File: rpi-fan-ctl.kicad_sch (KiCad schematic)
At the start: 21 parts, among them J2 Conn_01x05, Q1 NPN, Q2 NPN, Q3 NPN, Q4 NPN

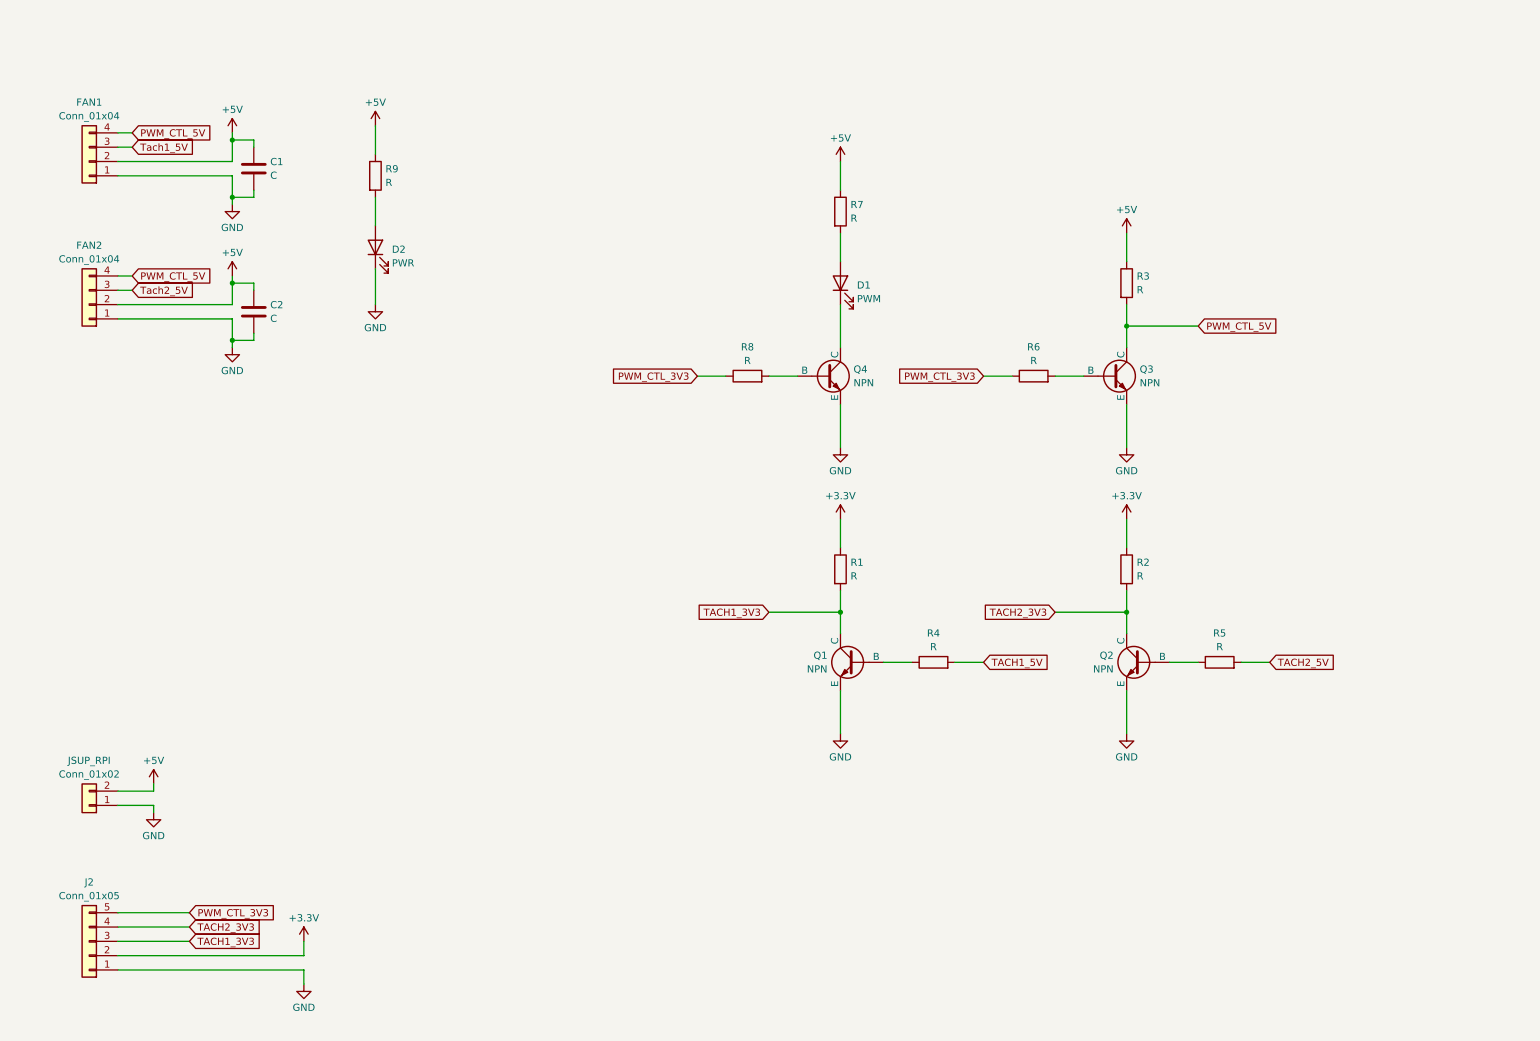
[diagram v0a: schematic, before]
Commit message: added footprints
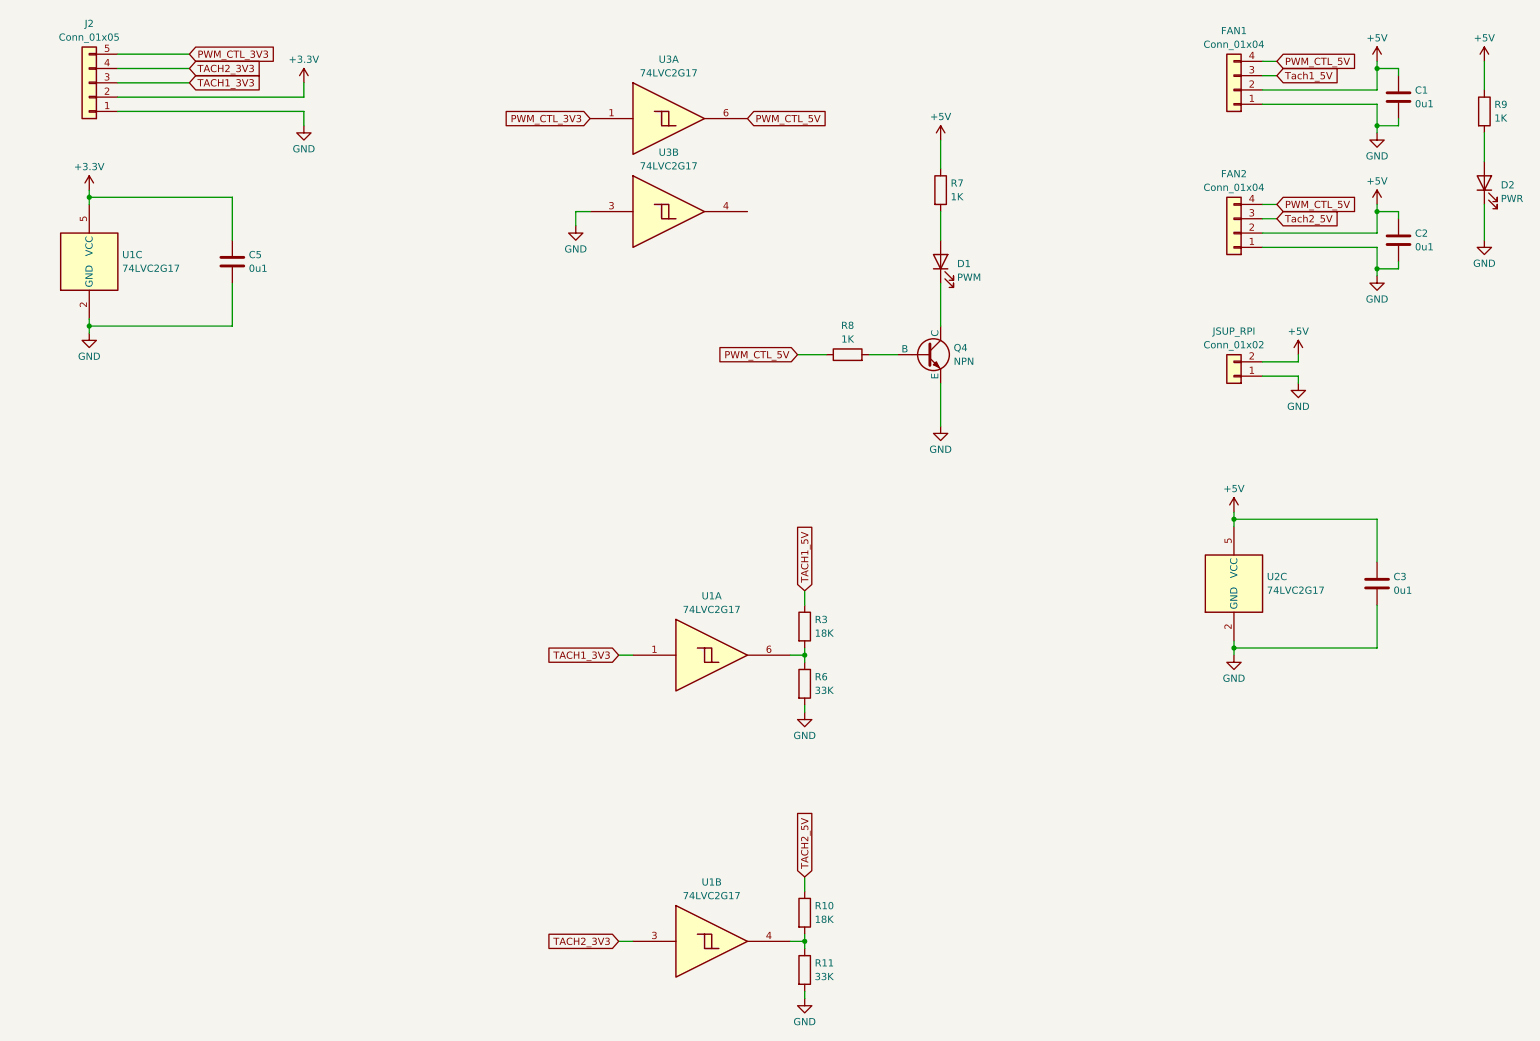
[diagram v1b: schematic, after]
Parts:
- removed Q1, Q2, Q3: NPN, symbol Simulation_SPICE:NPN
- removed R1, R2, R4, R5: R, symbol Device:R
- added C3, C5: 0u1, Capacitor_SMD:C_0603_1608Metric_Pad1.08x0.95mm_HandSolder, symbol Device:C
- added R10: 18K, Resistor_SMD:R_0603_1608Metric_Pad0.98x0.95mm_HandSolder, symbol Device:R
- added R11: 33K, Resistor_SMD:R_0603_1608Metric_Pad0.98x0.95mm_HandSolder, symbol Device:R
- added U1, U3: 74LVC2G17, Package_TO_SOT_SMD:SOT-363_SC-70-6_Handsoldering, symbol 74xGxx:74LVC2G17
- added U2: 74LVC2G17, symbol 74xGxx:74LVC2G17
- C1, C2: value C -> 0u1; footprint (none) -> Capacitor_SMD:C_0603_1608Metric_Pad1.08x0.95mm_HandSolder
- R3: value R -> 18K; footprint (none) -> Resistor_SMD:R_0603_1608Metric_Pad0.98x0.95mm_HandSolder
- R6: value R -> 33K; footprint (none) -> Resistor_SMD:R_0603_1608Metric_Pad0.98x0.95mm_HandSolder
- R7, R8, R9: value R -> 1K; footprint (none) -> Resistor_SMD:R_0603_1608Metric_Pad0.98x0.95mm_HandSolder
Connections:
- net +3.3V: now also C5.1, U1.5 (VCC)
- net +5V: now also C3.1, U2.5 (VCC); no longer R3.1
- net GND: now also R6.2, C3.2, C5.2, R11.2, U1.2 (GND), U2.2 (GND), U3.3
- net PWM_CTL_3V3: now also U3.1; no longer R6.1, R8.1
- net PWM_CTL_5V: now also R8.1, U3.6; no longer R3.2
- net TACH1_3V3: now also U1.1
- net TACH1_5V: now also R3.1
- net TACH2_3V3: now also U1.3
- net TACH2_5V: now also R10.1
- new net: R3.2, R6.1, U1.6
- new net: R10.2, R11.1, U1.4
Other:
- moved on the sheet: C1, C2, D1, D2, FAN1, FAN2, J2, JSUP_RPI, Q4, R7, R8, R9

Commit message: some routing progress
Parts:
- removed D1: PWM, symbol Device:LED
- removed D2: PWR, symbol Device:LED
- removed Q4: NPN, symbol Simulation_SPICE:NPN
- removed R8: 1K, Resistor_SMD:R_0603_1608Metric_Pad0.98x0.95mm_HandSolder, symbol Device:R
- added D1: D, Diode_SMD:D_SOD-123F, symbol Device:D
- added D2, D3, D5, D6: LTST-C191TBKT, Diode_SMD:D_0402_1005Metric_Pad0.77x0.64mm_HandSolder, symbol J-Link-SWD-rescue:LTST-C191TBKT-dk_LED-Indication-Discrete
- added D4: D, Diode_SMD:D_SOD-123, symbol Device:D
- added R1, R2, R3: 0R, Resistor_SMD:R_0603_1608Metric_Pad0.98x0.95mm_HandSolder, symbol Device:R
- added R6, R9: 1K, Resistor_SMD:R_0603_1608Metric_Pad0.98x0.95mm_HandSolder, symbol Device:R
- FAN1, FAN2: footprint (none) -> Connector_PinHeader_2.54mm:PinHeader_1x04_P2.54mm_Horizontal
- RPI1: renamed from J2; footprint (none) -> Connector_PinHeader_2.54mm:PinHeader_1x05_P2.54mm_Vertical
- SUP1: renamed from JSUP_RPI; footprint (none) -> Connector_PinHeader_2.54mm:PinHeader_1x02_P2.54mm_Horizontal
- U1: renamed from U3; footprint Package_TO_SOT_SMD:SOT-363_SC-70-6_Handsoldering -> Package_TO_SOT_SMD:SOT-23-6_Handsoldering; DigiKey https://www.digikey.de/en/products/detail/texas-instruments/SN74LVC2G17DCKR/479737 -> https://www.digikey.de/en/products/detail/texas-instruments/SN74LVC2G17DBVR/479735
- U1: renamed from U2; footprint (none) -> Package_TO_SOT_SMD:SOT-23-6_Handsoldering; DigiKey (none) -> https://www.digikey.de/en/products/detail/texas-instruments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
- U2: renamed from U1; footprint Package_TO_SOT_SMD:SOT-363_SC-70-6_Handsoldering -> Package_TO_SOT_SMD:SOT-23-6_Handsoldering; DigiKey https://www.digikey.de/en/products/detail/texas-instruments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 -> (none)
- U2: renamed from U1; footprint (none) -> Package_TO_SOT_SMD:SOT-23-6_Handsoldering
- renumbered C5 to C3, C3 to C4, R7 to R4, R9 to R5, R3 to R7, R6 to R8
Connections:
- net Tach1_5V is gone; now on net TACH1_5V: FAN1.3 (Pin_3)
- net Tach2_5V is gone; now on net TACH2_5V: FAN2.3 (Pin_3)
- net +5V: now also D1.1 (K), D4.1 (K); no longer R4.1
- net GND: now also D1.2 (A), D2.2, D3.2, D4.2 (A), D5.2, D6.2
- net PWM_CTL_3V3: now also R1.2; no longer RPI1.5 (Pin_5)
- net PWM_CTL_5V: now also R4.1
- net TACH1_3V3: now also U2.4, R3.2, R6.1; no longer RPI1.3 (Pin_3), U2.1
- net TACH2_3V3: now also U2.6, R2.2, R9.1; no longer RPI1.4 (Pin_4), U2.3
- net at R7.2, R8.1: now also U2.3; no longer U2.6
- net at R5.2: now also D3.1
- net at R10.2, R11.1: now also U2.1; no longer U2.4
- net at R4.2: now also D2.1
- new net: D5.1, R6.2
- new net: R1.1, RPI1.5 (Pin_5)
- new net: R3.1, RPI1.3 (Pin_3)
- new net: R2.1, RPI1.4 (Pin_4)
- new net: D6.1, R9.2
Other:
- moved on the sheet: C1, C2, FAN1, FAN2, R4, R5, U2A, U2B

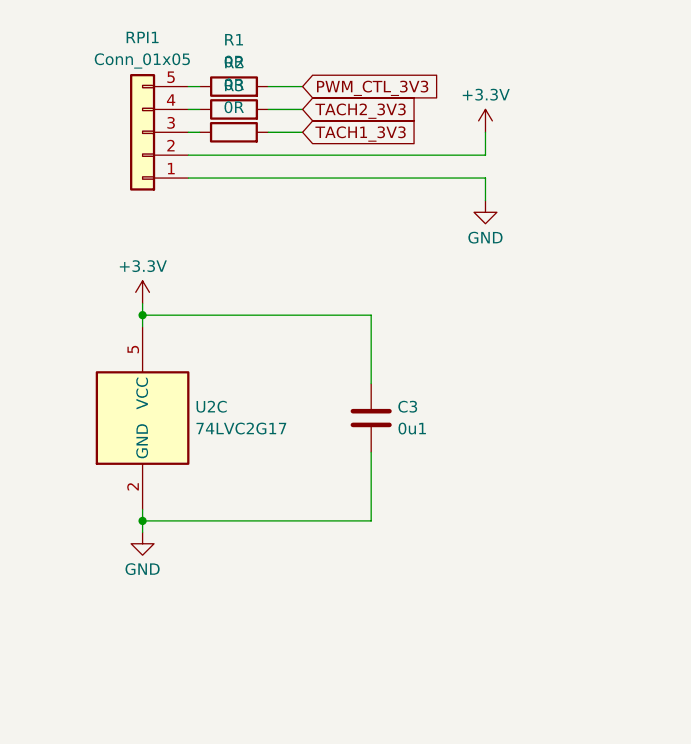
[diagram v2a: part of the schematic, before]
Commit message: made all preview connectors angled
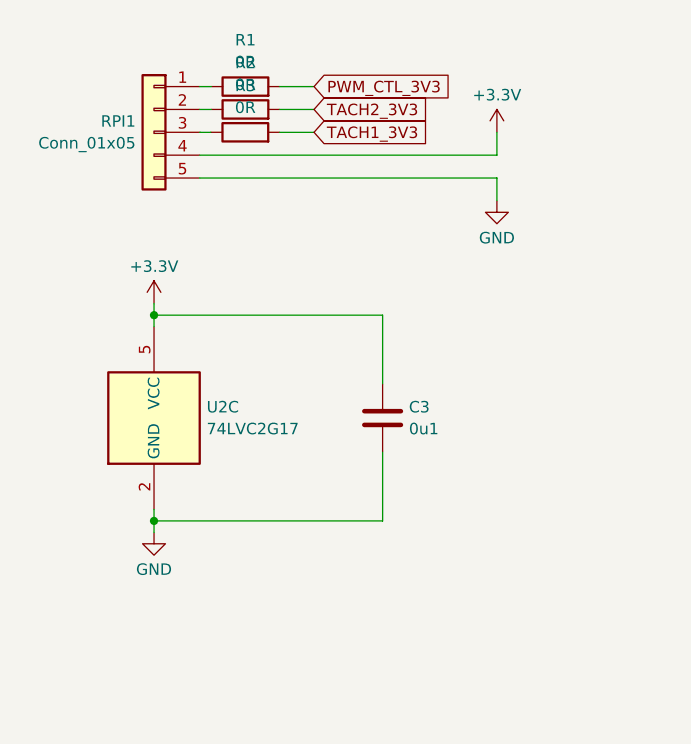
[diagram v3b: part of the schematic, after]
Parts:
- RPI1: footprint Connector_PinHeader_2.54mm:PinHeader_1x05_P2.54mm_Vertical -> Connector_PinHeader_2.54mm:PinHeader_1x05_P2.54mm_Horizontal
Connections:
- net +3.3V: now also RPI1.4 (Pin_4); no longer RPI1.2 (Pin_2)
- net GND: now also RPI1.5 (Pin_5); no longer RPI1.1 (Pin_1)
- net at R1.1: now also RPI1.1 (Pin_1); no longer RPI1.5 (Pin_5)
- net at R2.1: now also RPI1.2 (Pin_2); no longer RPI1.4 (Pin_4)
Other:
- moved on the sheet: C3, R1, R2, R3, RPI1, U2C

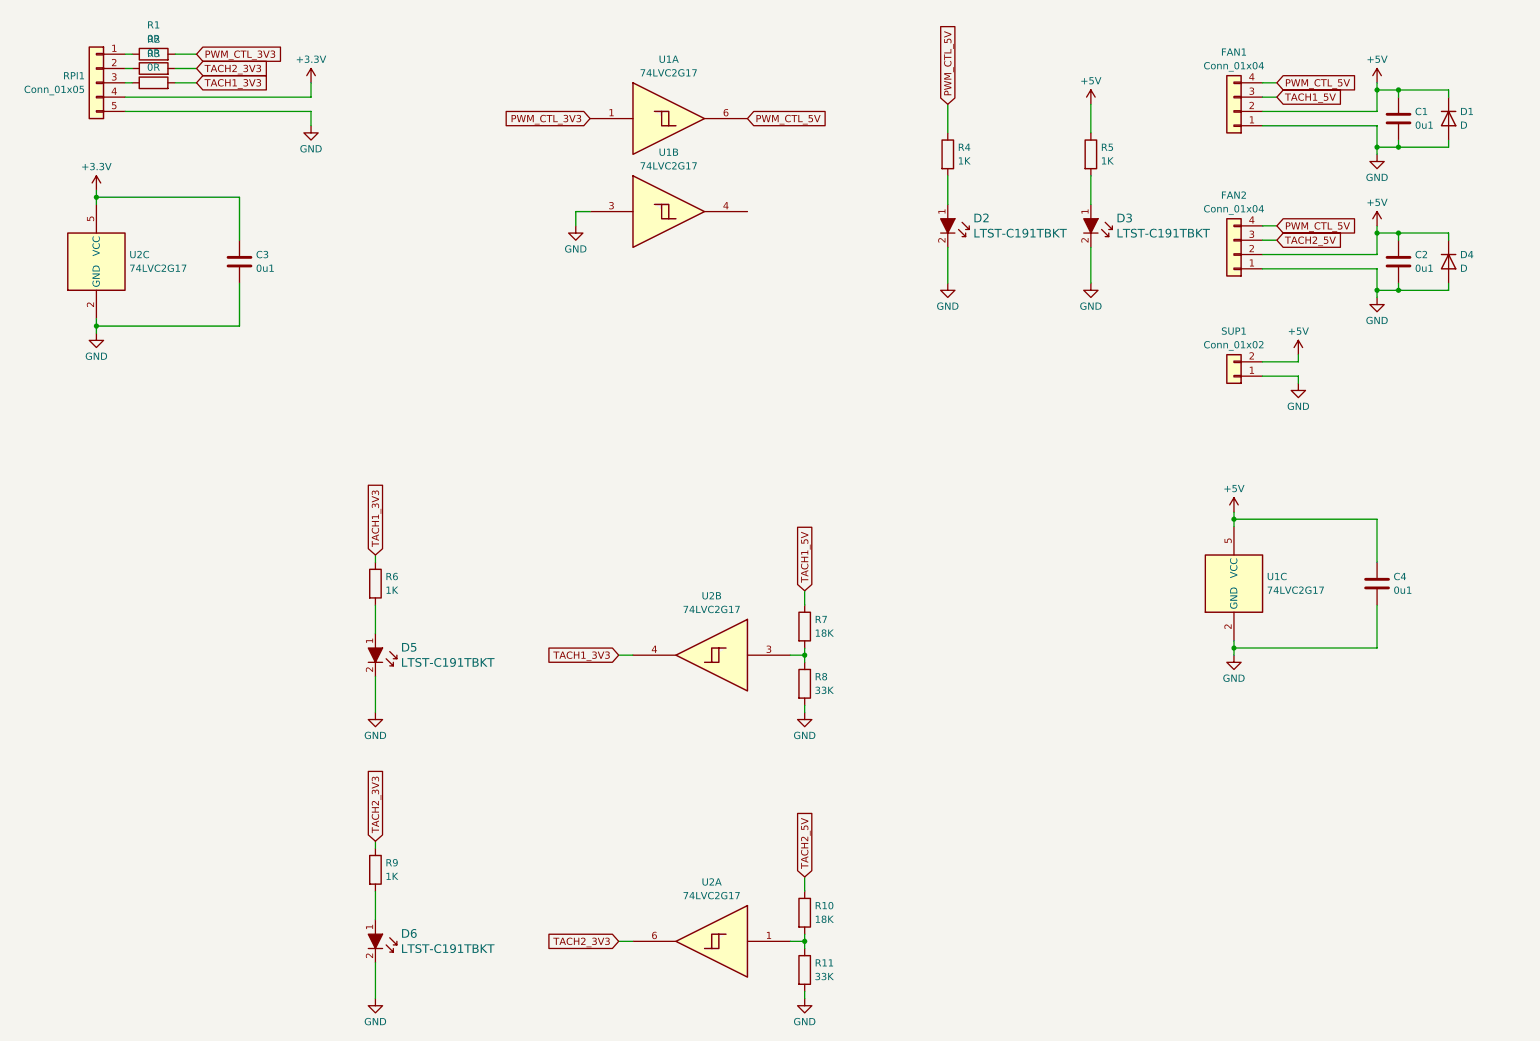
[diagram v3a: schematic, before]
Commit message: updated voltage level converter
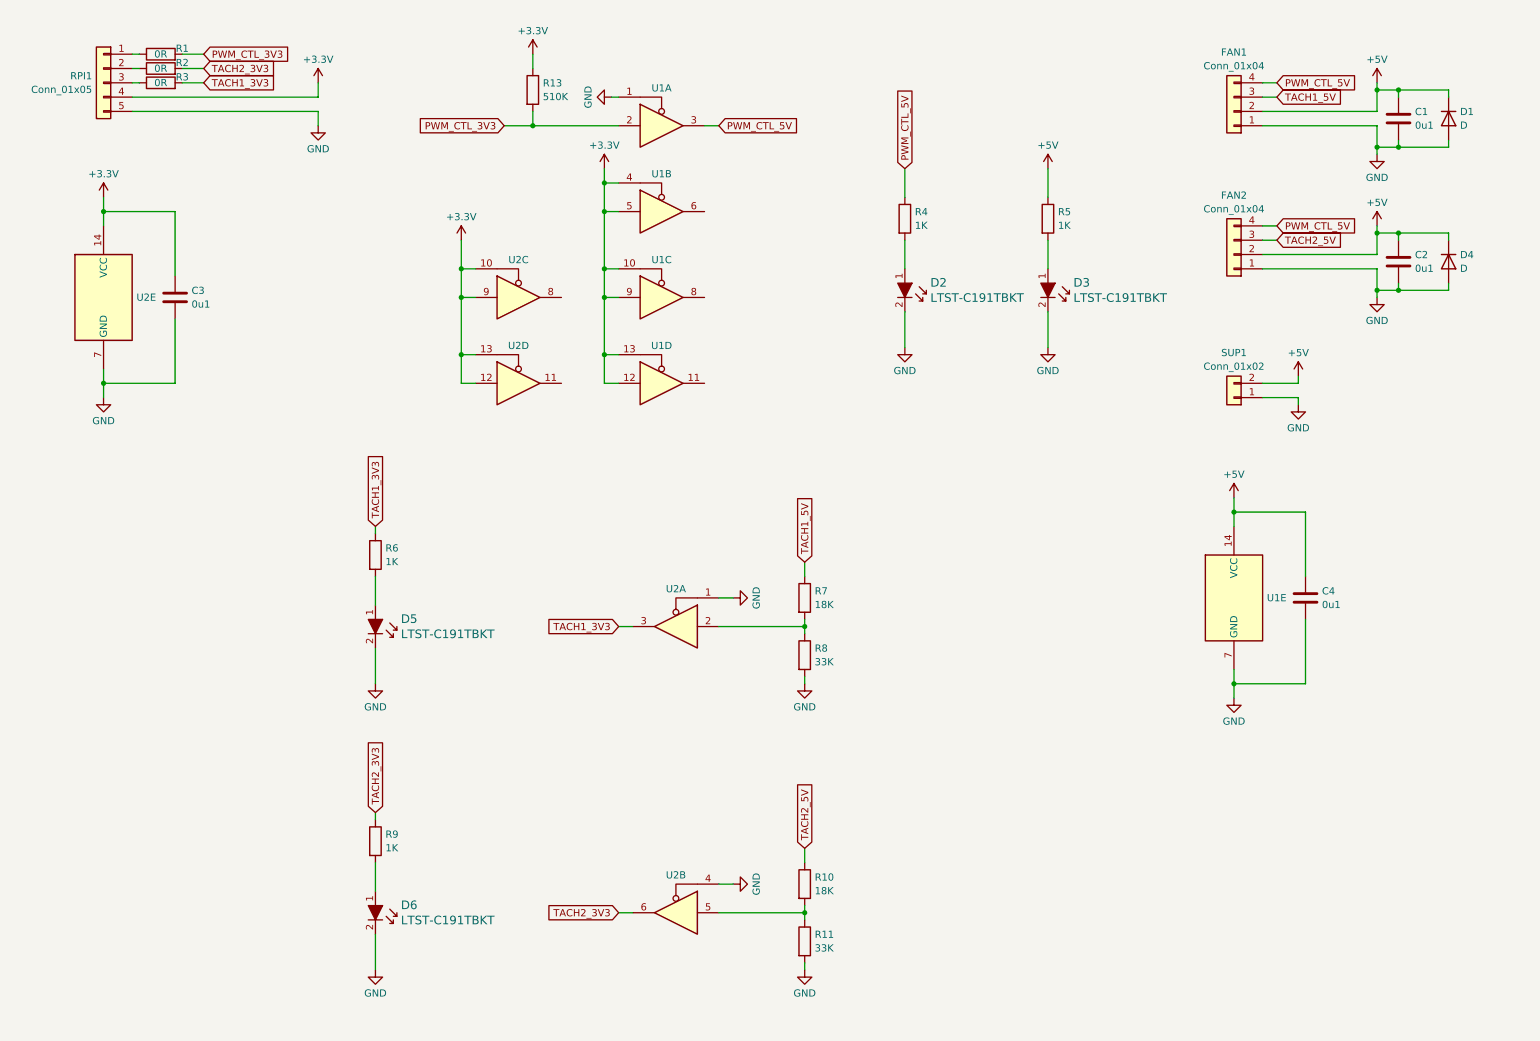
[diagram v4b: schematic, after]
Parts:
- removed U1, U2: 74LVC2G17, Package_TO_SOT_SMD:SOT-23-6_Handsoldering, symbol 74xGxx:74LVC2G17
- added R13: 510K, Resistor_SMD:R_0603_1608Metric_Pad0.98x0.95mm_HandSolder, symbol Device:R
- added U1, U2: SN74HCT125DR, Package_SO:SOIC-14_3.9x8.7mm_P1.27mm, symbol fanctl:SN74HCT125DR
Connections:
- net +3.3V: now also R13.1, U1.10, U1.12, U1.13, U1.4, U1.5, U1.9, U2.10, U2.12, U2.13, U2.14 (VCC), U2.9
- net +5V: now also U1.14 (VCC)
- net GND: now also U1.1, U1.7 (GND), U2.1, U2.4, U2.7 (GND)
- net PWM_CTL_3V3: now also R13.2, U1.2
- net PWM_CTL_5V: now also U1.3
- net TACH1_3V3: now also U2.3
- net TACH2_3V3: now also U2.6
- net at R7.2, R8.1: now also U2.2
- net at R10.2, R11.1: now also U2.5
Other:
- moved on the sheet: C3, C4, D2, D3, D5, D6, R1, R10, R11, R2, R3, R4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
